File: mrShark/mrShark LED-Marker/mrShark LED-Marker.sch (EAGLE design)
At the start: 38 parts, among them CON1 DF12-20DS, IC1 PCA9552PW

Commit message: Updated LED-marker to version 0.0.1
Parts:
- LED2: value (none) -> LW L283
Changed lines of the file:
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@@
 <setting verticaltext="up"/>
 </settings>
-<grid distance="0.1" unitdist="inch" unit="inch" style="lines" multiple="1" display="no" altdistance="0.01" altunitdist="inch" altunit="inch"/>
+<grid distance="0.1" unitdist="inch" unit="inch" style="lines" multiple="1" display="yes" altdistance="0.01" altunitdist="inch" altunit="inch"/>
 <layers>
 <layer number="1" name="Top" color="4" fill="1" visible="no" active="no"/>
@@
 <part name="P+5" library="supply1" deviceset="VCC" device=""/>
 <part name="LED1" library="led" deviceset="LED" device="CHIPLED_0603"/>
-<part name="LED2" library="led" deviceset="LED" device="CHIPLED_0603"/>
+<part name="LED2" library="led" deviceset="LED" device="CHIPLED_0603" value="LW L283"/>
 <part name="LED3" library="led" deviceset="LED" device="CHIPLED_0603"/>
 <part name="LED4" library="led" deviceset="LED" device="CHIPLED_0603"/>

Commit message: Updated LED-marker
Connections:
- net GND: no longer CON1.16
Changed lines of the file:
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@@
 <pinref part="CON1" gate="CON$1" pin="15"/>
 <wire x1="167.64" y1="53.34" x2="172.72" y2="53.34" width="0.1524" layer="91"/>
-<wire x1="172.72" y1="53.34" x2="172.72" y2="55.88" width="0.1524" layer="91"/>
-<pinref part="CON1" gate="CON$1" pin="16"/>
-<wire x1="172.72" y1="55.88" x2="167.64" y2="55.88" width="0.1524" layer="91"/>
 <pinref part="CON1" gate="CON$1" pin="12"/>
 <wire x1="167.64" y1="45.72" x2="172.72" y2="45.72" width="0.1524" layer="91"/>
 <wire x1="172.72" y1="45.72" x2="172.72" y2="53.34" width="0.1524" layer="91"/>
-<junction x="172.72" y="53.34"/>
 <pinref part="GND3" gate="1" pin="GND"/>
 <wire x1="172.72" y1="45.72" x2="172.72" y2="38.1" width="0.1524" layer="91"/>

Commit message: Added switchable position lights
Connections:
- new net POS_LIGHT: IC1.LED9, LED19.C, LED20.C, LED21.C, LED22.C
- net GND: no longer LED19.C, LED20.C, LED21.C, LED22.C
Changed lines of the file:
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@@
 <part name="P+15" library="supply1" deviceset="VCC" device=""/>
 <part name="P+16" library="supply1" deviceset="VCC" device=""/>
-<part name="GND5" library="supply1" deviceset="GND" device=""/>
-<part name="GND6" library="supply1" deviceset="GND" device=""/>
-<part name="GND7" library="supply1" deviceset="GND" device=""/>
-<part name="GND8" library="supply1" deviceset="GND" device=""/>
 </parts>
 <sheets>
@@
 <instance part="P+15" gate="VCC" x="233.68" y="83.82"/>
 <instance part="P+16" gate="VCC" x="213.36" y="83.82"/>
-<instance part="GND5" gate="1" x="208.28" y="35.56"/>
-<instance part="GND6" gate="1" x="218.44" y="35.56"/>
-<instance part="GND7" gate="1" x="228.6" y="35.56"/>
-<instance part="GND8" gate="1" x="238.76" y="35.56"/>
 </instances>
 <busses>
@@
 <junction x="35.56" y="116.84"/>
 </segment>
-<segment>
-<pinref part="LED20" gate="G$1" pin="C"/>
-<wire x1="208.28" y1="38.1" x2="208.28" y2="48.26" width="0.1524" layer="91"/>
-<pinref part="LED19" gate="G$1" pin="C"/>
-<wire x1="218.44" y1="38.1" x2="218.44" y2="48.26" width="0.1524" layer="91"/>
-<pinref part="GND5" gate="1" pin="GND"/>
-<pinref part="GND6" gate="1" pin="GND"/>
-</segment>
-<segment>
-<pinref part="LED22" gate="G$1" pin="C"/>
-<wire x1="228.6" y1="38.1" x2="228.6" y2="48.26" width="0.1524" layer="91"/>
-<pinref part="LED21" gate="G$1" pin="C"/>
-<wire x1="238.76" y1="38.1" x2="238.76" y2="48.26" width="0.1524" layer="91"/>
-<pinref part="GND7" gate="1" pin="GND"/>
-<pinref part="GND8" gate="1" pin="GND"/>
-</segment>
 </net>
 <net name="INT1" class="0">
@@
 </segment>
 </net>
+<net name="POS_LIGHT" class="0">
+<segment>
+<pinref part="IC1" gate="IC1" pin="LED9"/>
+<wire x1="63.5" y1="104.14" x2="68.58" y2="104.14" width="0.1524" layer="91"/>
+<label x="68.58" y="104.14" size="1.27" layer="95" xref="yes"/>
+</segment>
+<segment>
+<pinref part="LED20" gate="G$1" pin="C"/>
+<wire x1="208.28" y1="43.18" x2="208.28" y2="48.26" width="0.1524" layer="91"/>
+<pinref part="LED19" gate="G$1" pin="C"/>
+<wire x1="218.44" y1="43.18" x2="218.44" y2="48.26" width="0.1524" layer="91"/>
+<label x="208.28" y="43.18" size="1.27" layer="95" rot="R270" xref="yes"/>
+<label x="218.44" y="43.18" size="1.27" layer="95" rot="R270" xref="yes"/>
+</segment>
+<segment>
+<pinref part="LED22" gate="G$1" pin="C"/>
+<wire x1="228.6" y1="43.18" x2="228.6" y2="48.26" width="0.1524" layer="91"/>
+<pinref part="LED21" gate="G$1" pin="C"/>
+<wire x1="238.76" y1="43.18" x2="238.76" y2="48.26" width="0.1524" layer="91"/>
+<label x="228.6" y="43.18" size="1.27" layer="95" rot="R270" xref="yes"/>
+<label x="238.76" y="43.18" size="1.27" layer="95" rot="R270" xref="yes"/>
+</segment>
+</net>

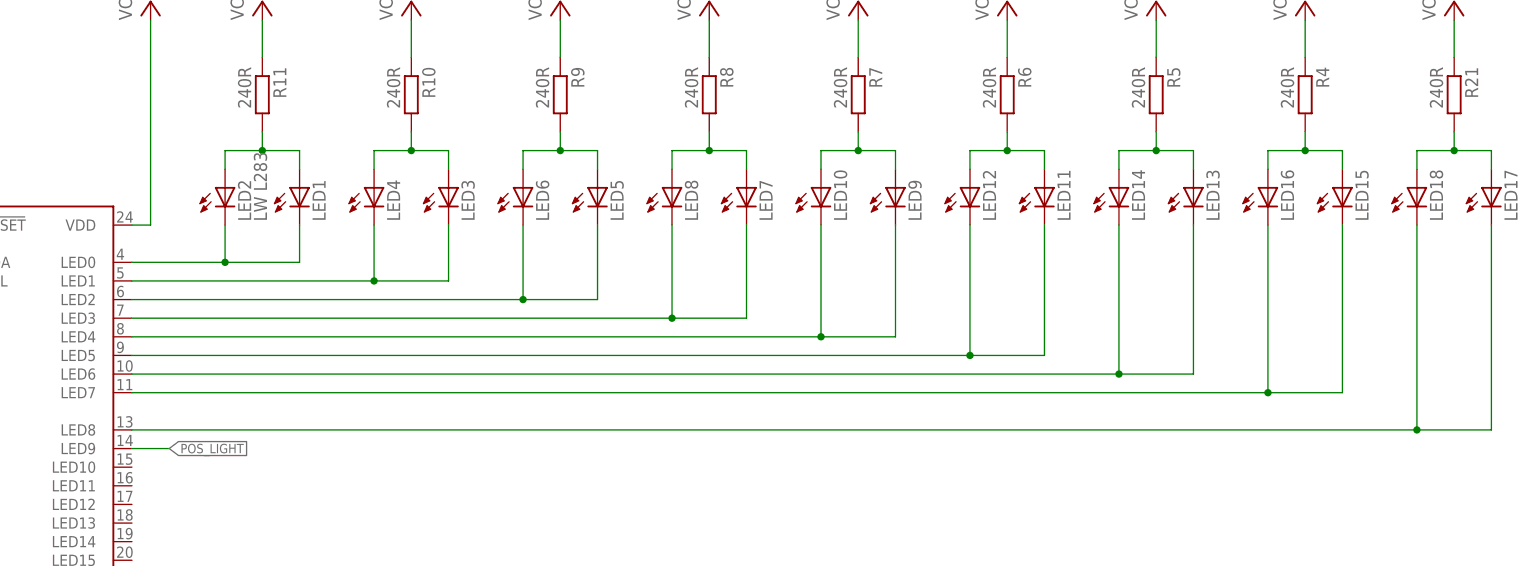
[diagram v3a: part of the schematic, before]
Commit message: Updated mrShark 1.2 & 1.3 Updated mrShark Adapter Updated mrShark LED-Marker to version 0.0.3
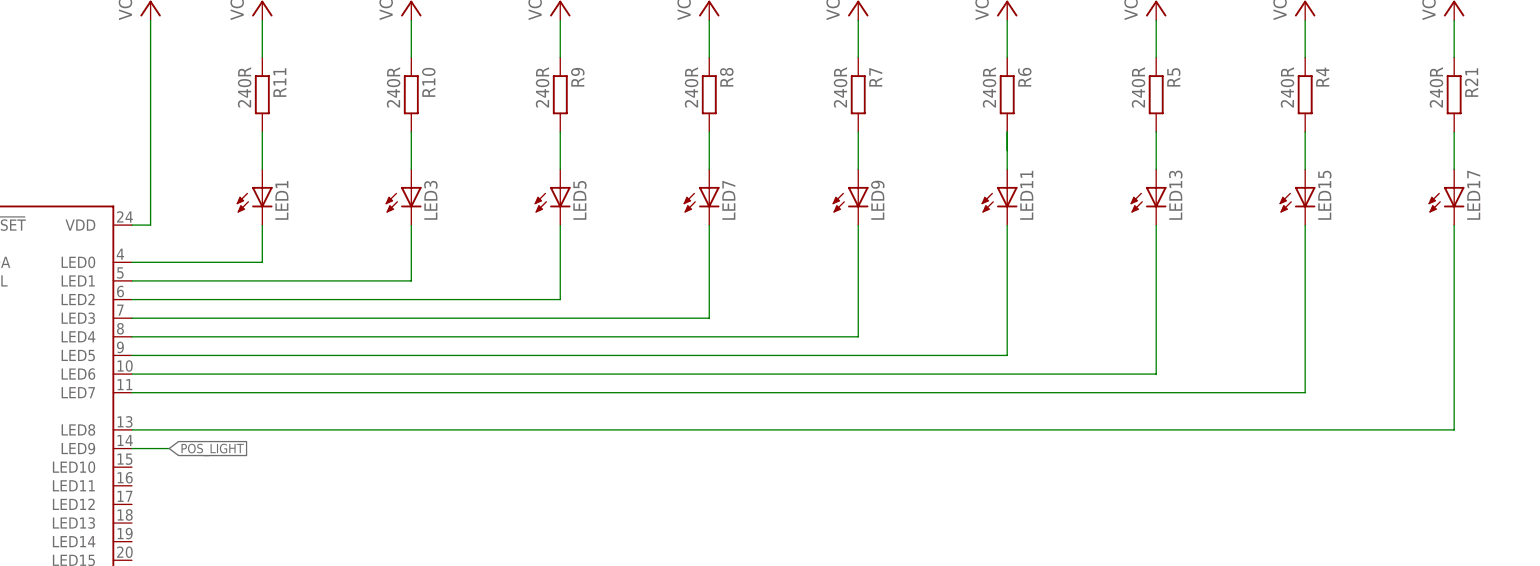
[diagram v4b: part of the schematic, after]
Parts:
- removed LED10, LED12, LED14, LED16, LED18, LED4, LED6, LED8: (no value), led:LEDCHIPLED_0603
- removed LED2: LW L283, led:LEDCHIPLED_0603
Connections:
- net N$10: no longer LED6.A
- net N$11: no longer LED4.A
- net N$12: no longer LED2.A
- net N$13: no longer LED2.C
- net N$14: no longer LED4.C
- net N$15: no longer LED6.C
- net N$16: no longer LED8.C
- net N$17: no longer LED10.C
- net N$18: no longer LED12.C
- net N$19: no longer LED14.C
- net N$2: no longer LED18.A
- net N$20: no longer LED16.C
- net N$21: no longer LED18.C
- net N$4: no longer LED16.A
- net N$5: no longer LED14.A
- net N$6: no longer LED12.A
- net N$7: no longer LED10.A
- net N$8: no longer LED8.A
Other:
- moved on the sheet: LED1, LED11, LED13, LED15, LED17, LED3, LED5, LED7, LED9
